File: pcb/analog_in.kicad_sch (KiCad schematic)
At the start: 16 parts, among them J7 Guitar Input, J8 Guitar Output, U5 TL072

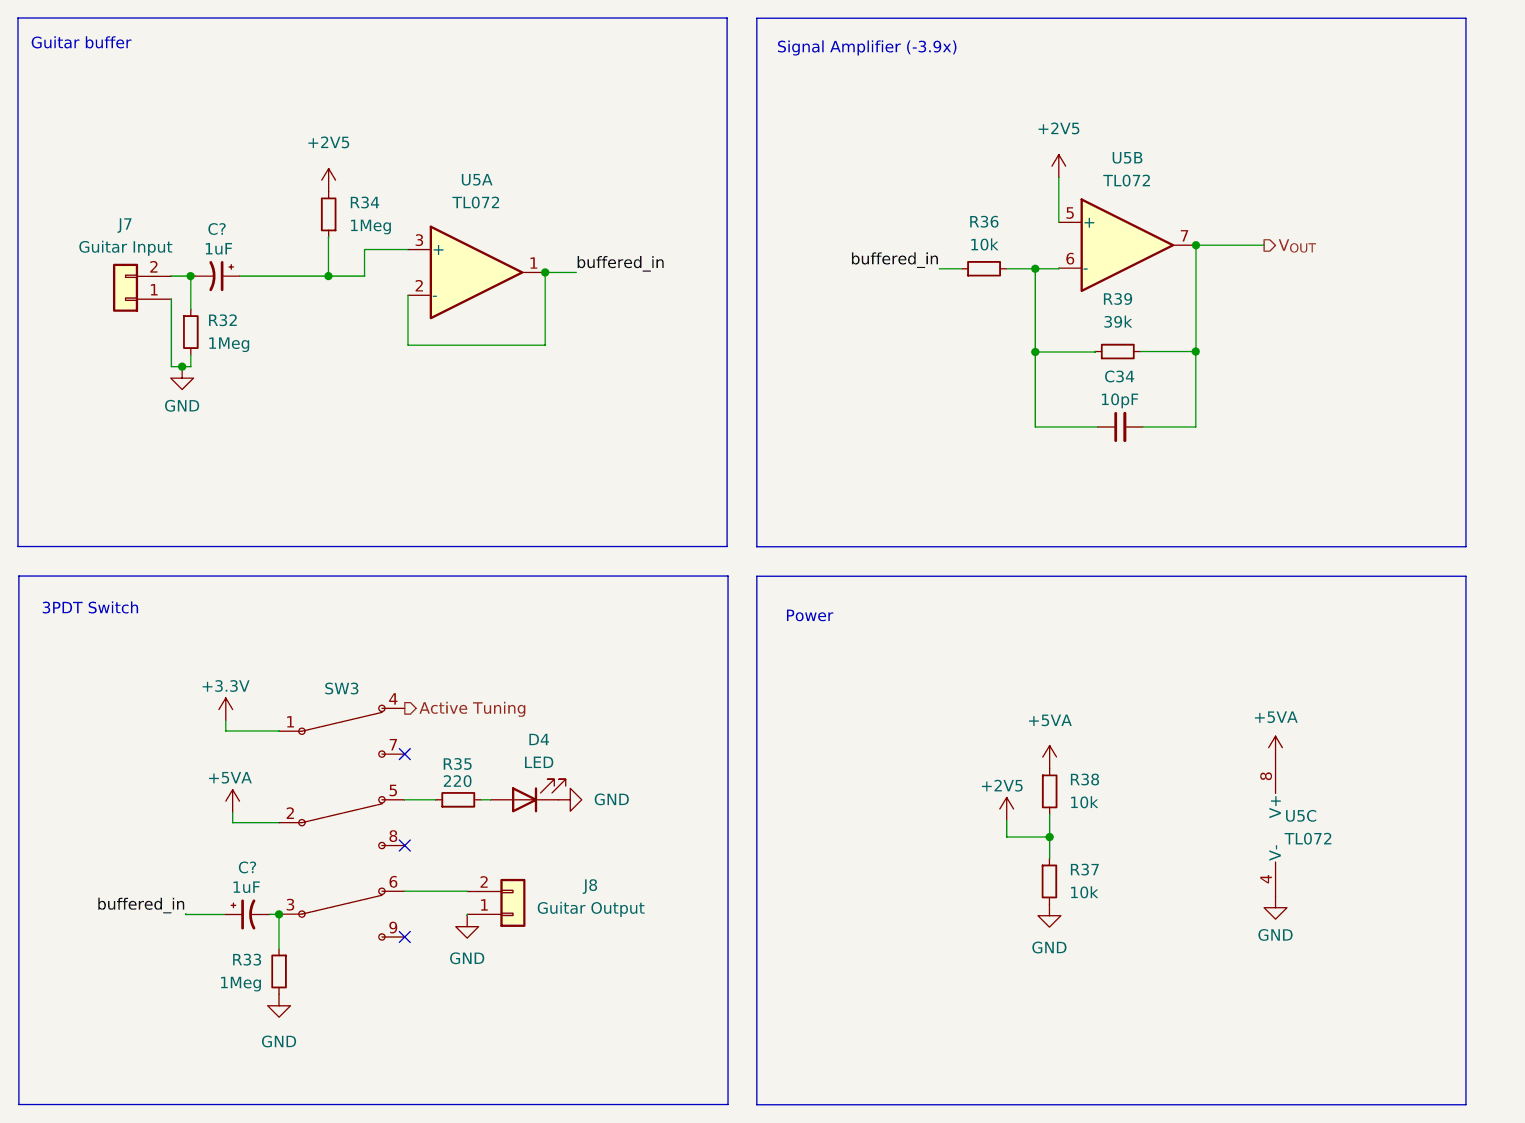
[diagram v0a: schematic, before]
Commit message: Adding safety to output jack signal path
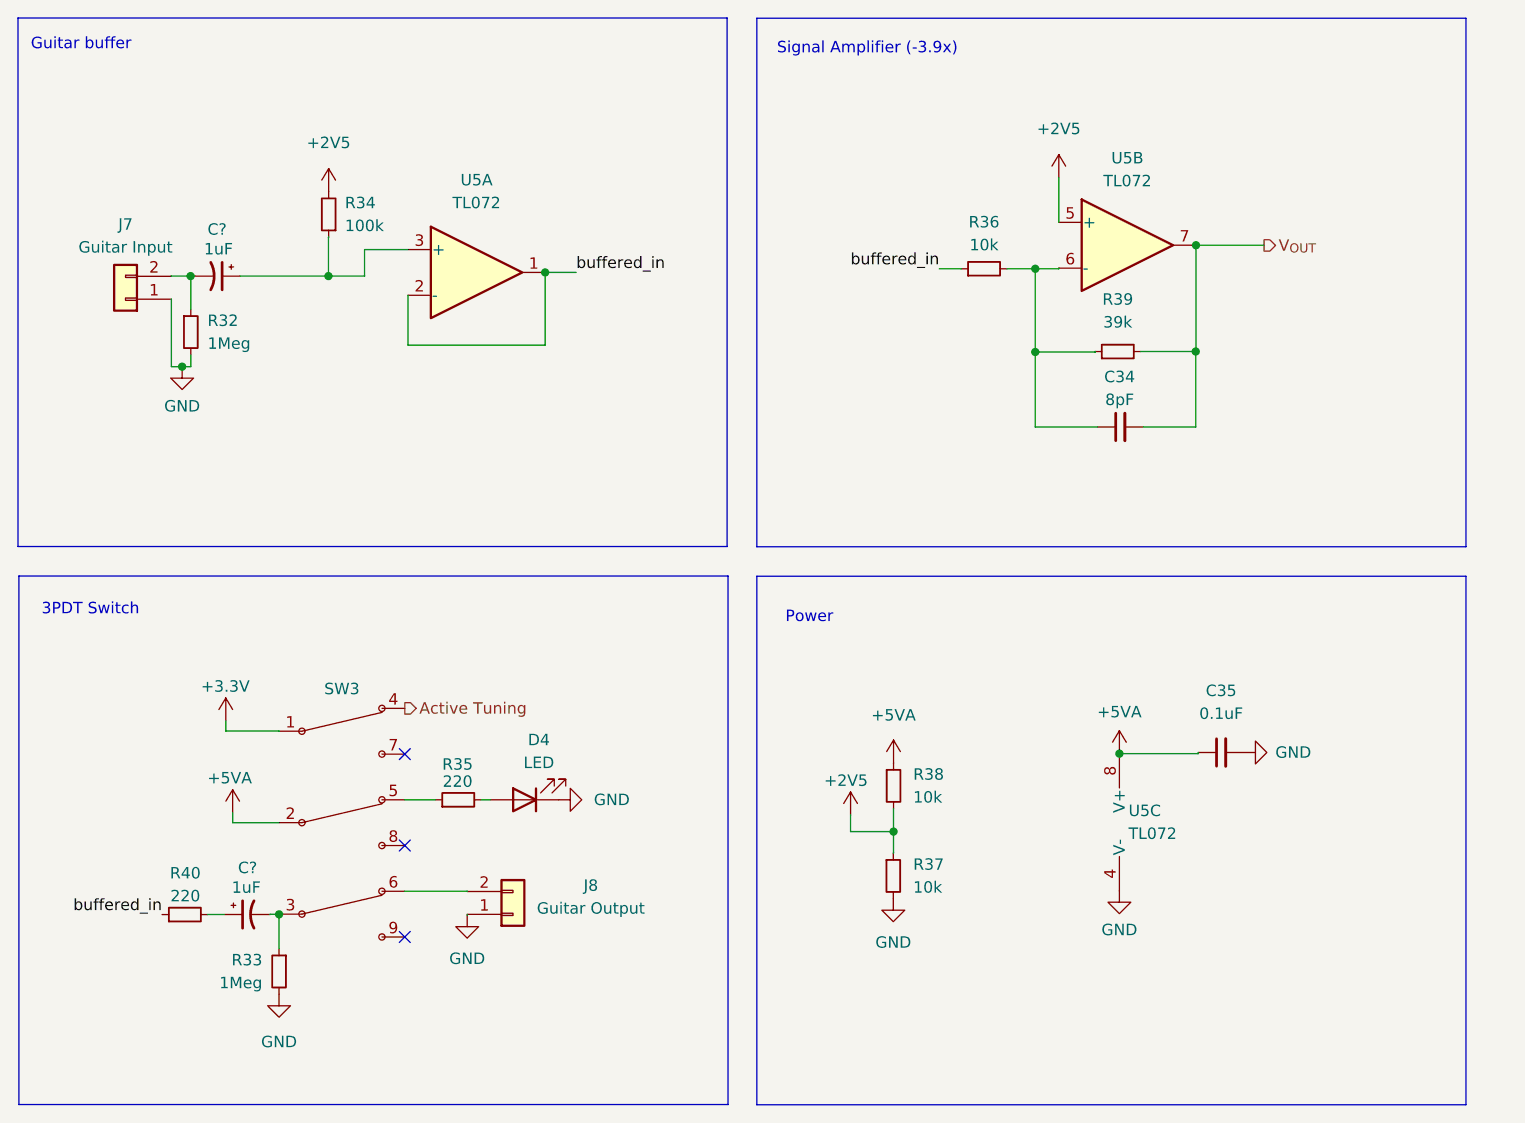
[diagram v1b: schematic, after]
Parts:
- added C35: 0.1uF, symbol Device:C_Small
- added R40: 220, symbol Device:R_Small
- C34: value 10pF -> 8pF
- R34: value 1Meg -> 100k
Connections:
- net +5VA: now also C35.1
- net GND: now also C35.2
- net buffered_in: now also R40.1; no longer C?.1
- new net: C?.1, R40.2
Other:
- moved on the sheet: R37, R38, U5C

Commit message: Assigned footprints and jlcpcb part number to all components
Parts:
- C34: footprint (none) -> Capacitor_SMD:C_0603_1608Metric; LCSC (none) -> C346204; MPN (none) -> CL10C080DB81PNC; Manufacturer (none) -> Samsung Electro-Mechanics
- C35: footprint (none) -> Capacitor_SMD:C_1206_3216Metric; LCSC (none) -> C577121; MPN (none) -> CC1206JKNPO9BN104; Manufacturer (none) -> Yageo
- C? (x2): footprint (none) -> Capacitor_SMD:C_0805_2012Metric; LCSC (none) -> C1712; MPN (none) -> CL21B105KAFNFNE; Manufacturer (none) -> Samsung Electro-Mechanics
- D4: footprint (none) -> Connector_PinHeader_2.54mm:PinHeader_1x02_P2.54mm_Vertical
- R32, R33: footprint (none) -> Resistor_SMD:R_0603_1608Metric; LCSC (none) -> C105578; MPN (none) -> RC0603FR-071ML; Manufacturer (none) -> Yageo
- R34: footprint (none) -> Resistor_SMD:R_0603_1608Metric; LCSC (none) -> C14675; MPN (none) -> RC0603FR-07100KL; Manufacturer (none) -> Yageo
- R35, R40: footprint (none) -> Resistor_SMD:R_0603_1608Metric; LCSC (none) -> C107696; MPN (none) -> RC0603FR-07220RL; Manufacturer (none) -> Yageo
- R36, R37, R38: footprint (none) -> Resistor_SMD:R_0603_1608Metric; LCSC (none) -> C98220; MPN (none) -> RC0603FR-0710KL; Manufacturer (none) -> Yageo
- R39: footprint (none) -> Resistor_THT:R_Axial_DIN0207_L6.3mm_D2.5mm_P7.62mm_Horizontal; LCSC (none) -> C173011; MPN (none) -> MFR-25FTE52-39K; Manufacturer (none) -> Yageo
- U5: footprint Package_DIP:DIP-8_W7.62mm_SMDSocket_SmallPads -> Package_DIP:DIP-8_W7.62mm_Socket; DNP (none) -> DNP

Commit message: Changed 10k inverting amp resistor to THT for easy swapping
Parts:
- R36: footprint Resistor_SMD:R_0603_1608Metric -> Resistor_THT:R_Axial_DIN0207_L6.3mm_D2.5mm_P7.62mm_Horizontal; LCSC C98220 -> C172967; MPN RC0603FR-0710KL -> MFR-25FTE52-10K
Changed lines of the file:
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@@
       (effects (font (size 1.27 1.27)))
     )
-    (property "Footprint" "Resistor_SMD:R_0603_1608Metric" (at 176.4284 60.9092 0)
+    (property "Footprint" "Resistor_THT:R_Axial_DIN0207_L6.3mm_D2.5mm_P7.62mm_Horizontal" (at 176.4284 60.9092 0)
       (effects (font (size 1.27 1.27)) hide)
     )
@@
       (effects (font (size 1.27 1.27)) hide)
     )
-    (property "MPN" "RC0603FR-0710KL" (at 176.4284 60.9092 0)
+    (property "MPN" "MFR-25FTE52-10K" (at 176.4284 60.9092 0)
       (effects (font (size 1.27 1.27)) hide)
     )
@@
       (effects (font (size 1.27 1.27)) hide)
     )
-    (property "LCSC" "C98220" (at 176.4284 60.9092 0)
+    (property "LCSC" "C172967" (at 176.4284 60.9092 0)
       (effects (font (size 1.27 1.27)) hide)
     )

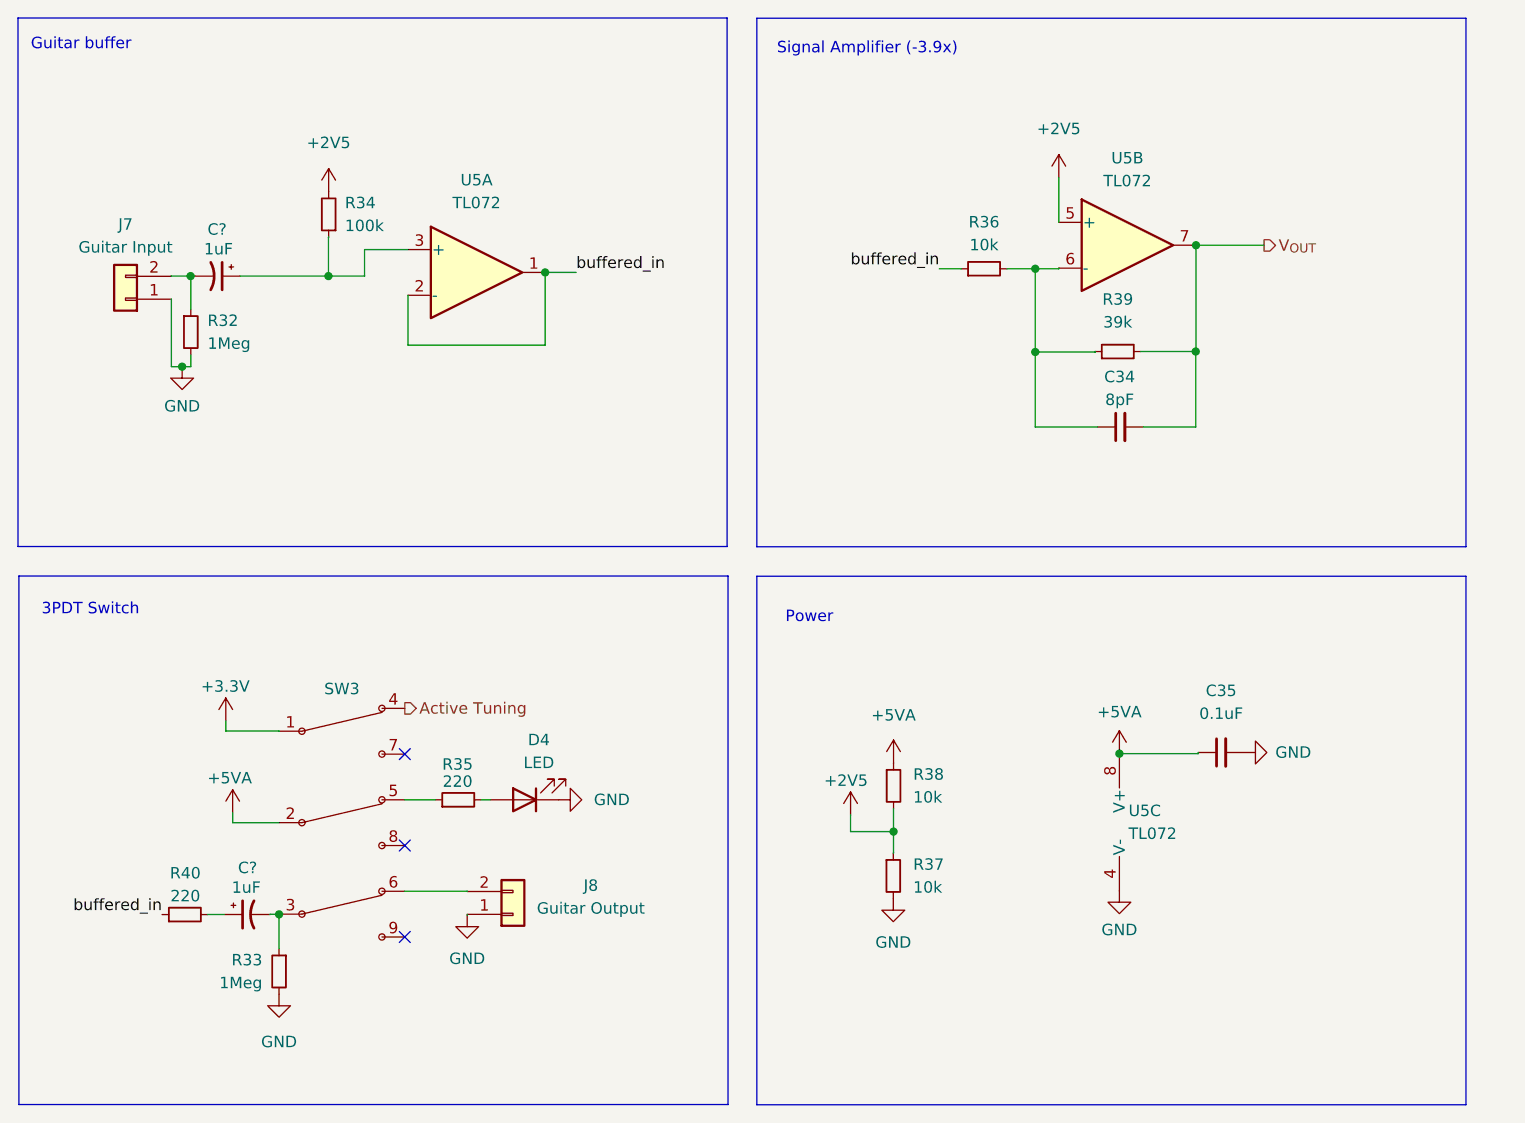
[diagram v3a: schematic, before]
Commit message: Changed op amp supply to 9V to make sure clipping doesn't occur
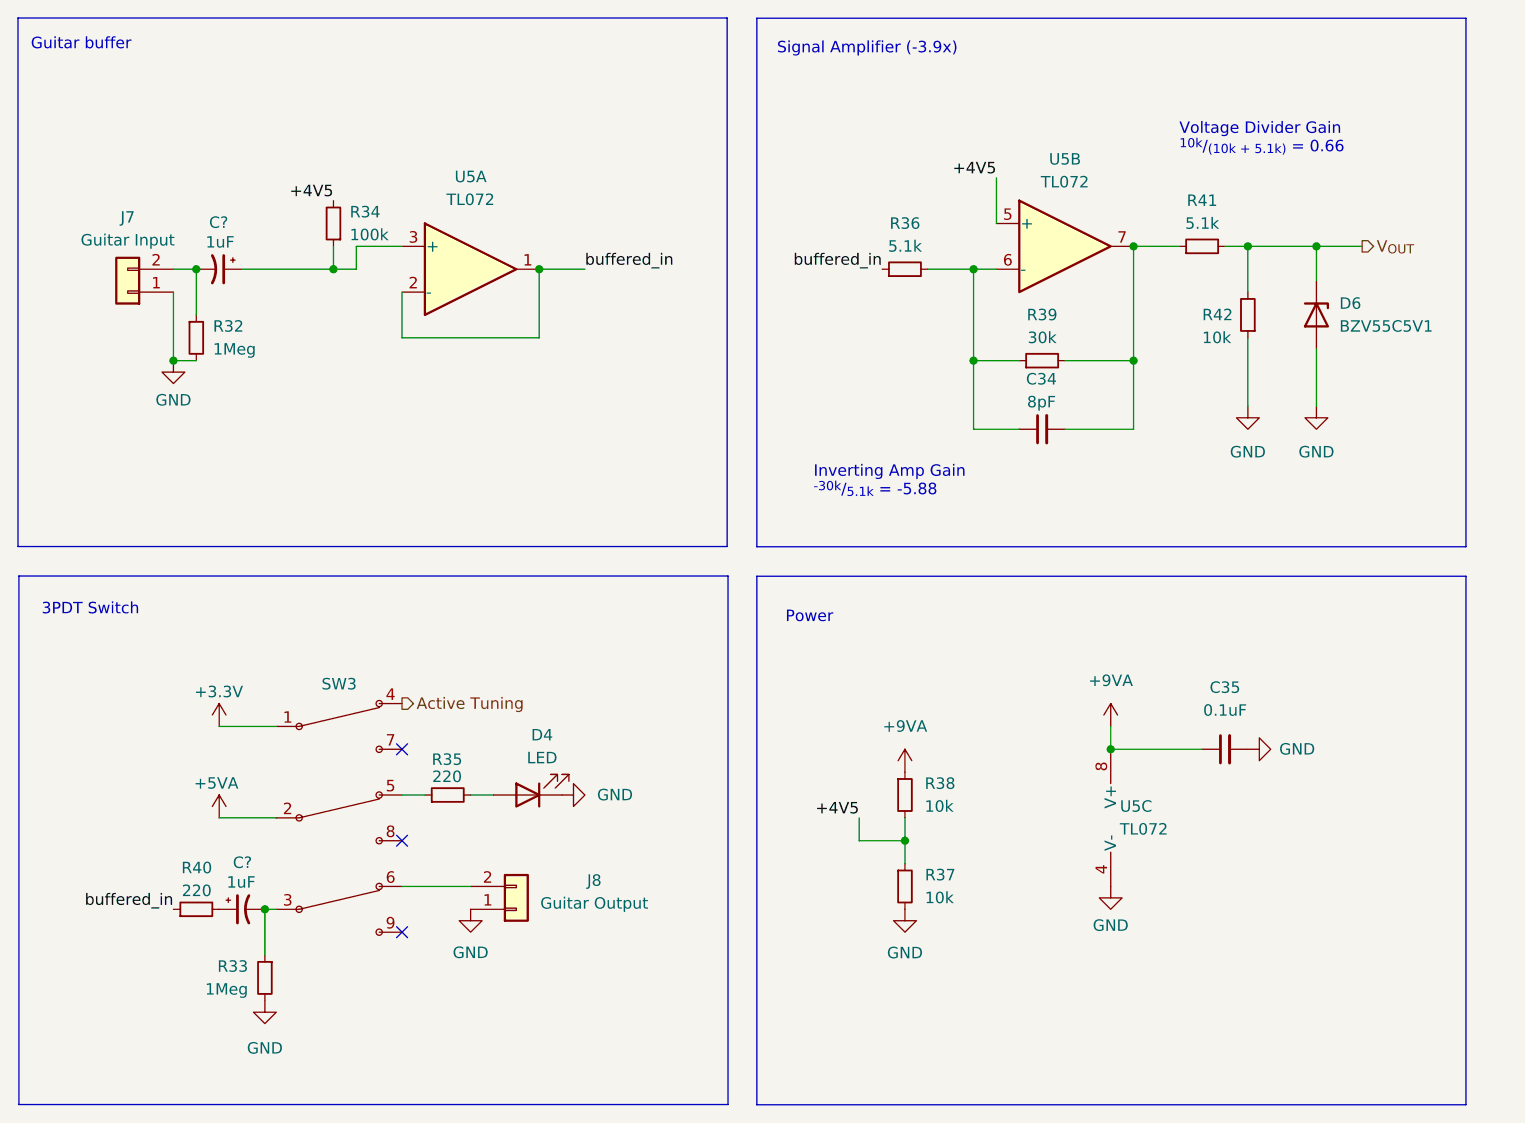
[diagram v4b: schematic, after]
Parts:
- added D6: BZV55C5V1, Diode_SMD:D_MiniMELF, symbol Diode:BZV55C5V1
- added R41: 5.1k, Resistor_SMD:R_0603_1608Metric, symbol Device:R_Small
- added R42: 10k, Resistor_SMD:R_0603_1608Metric, symbol Device:R_Small
- R36: value 10k -> 5.1k; LCSC C172967 -> C173033; MPN MFR-25FTE52-10K -> MFR-25FTE52-5K1
- R39: value 39k -> 30k; LCSC C173011 -> C173003; MPN MFR-25FTE52-39K -> MFR-25FTE52-30K
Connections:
- net +5VA: no longer C35.1, R38.1, U5.8 (V+)
- net GND: now also D6.2 (A), R42.1
- net V_{OUT}: now also D6.1 (K), R41.2, R42.2; no longer C34.2, R39.2, U5.7
- net +2V5 renamed +4V5
- new net: C34.2, R39.2, R41.1, U5.7
- new net +9VA: C35.1, R38.1, U5.8 (V+)
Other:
- note added: "Inverting Amp Gain ^{-30k}/_{5.1k} = -5.88"
- note added: "Voltage Divider Gain ^{10k}/_{(10k + 5.1k)} = 0.66"
- moved on the sheet: C34, C35, C?, D4, J7, J8, R32, R33, R34, R35, R36, R37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
